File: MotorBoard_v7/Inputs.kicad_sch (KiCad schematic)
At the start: 5 parts, among them J13 Bump_Left, J14 Bump_Center, J15 Bump_Right, U5 ESP8266-1

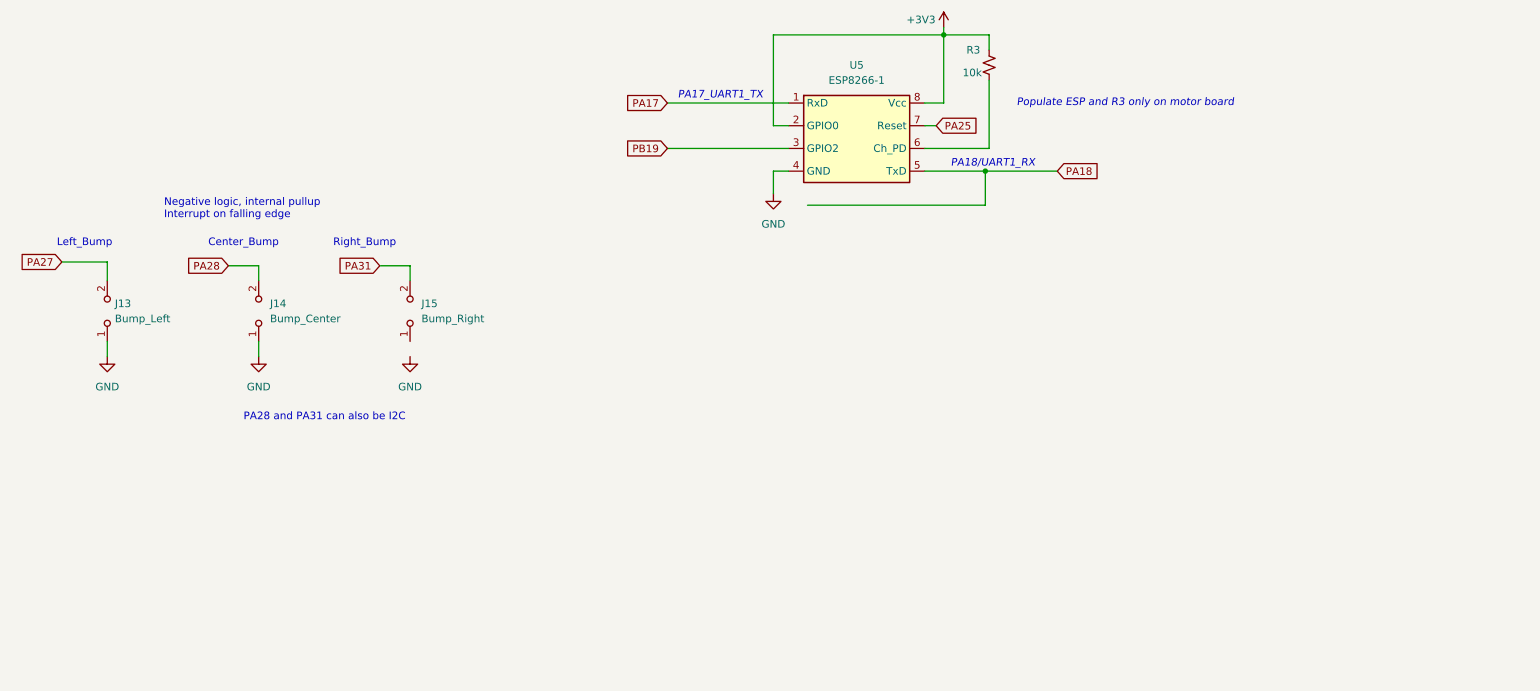
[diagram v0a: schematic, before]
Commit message: added lab 6 update starter files
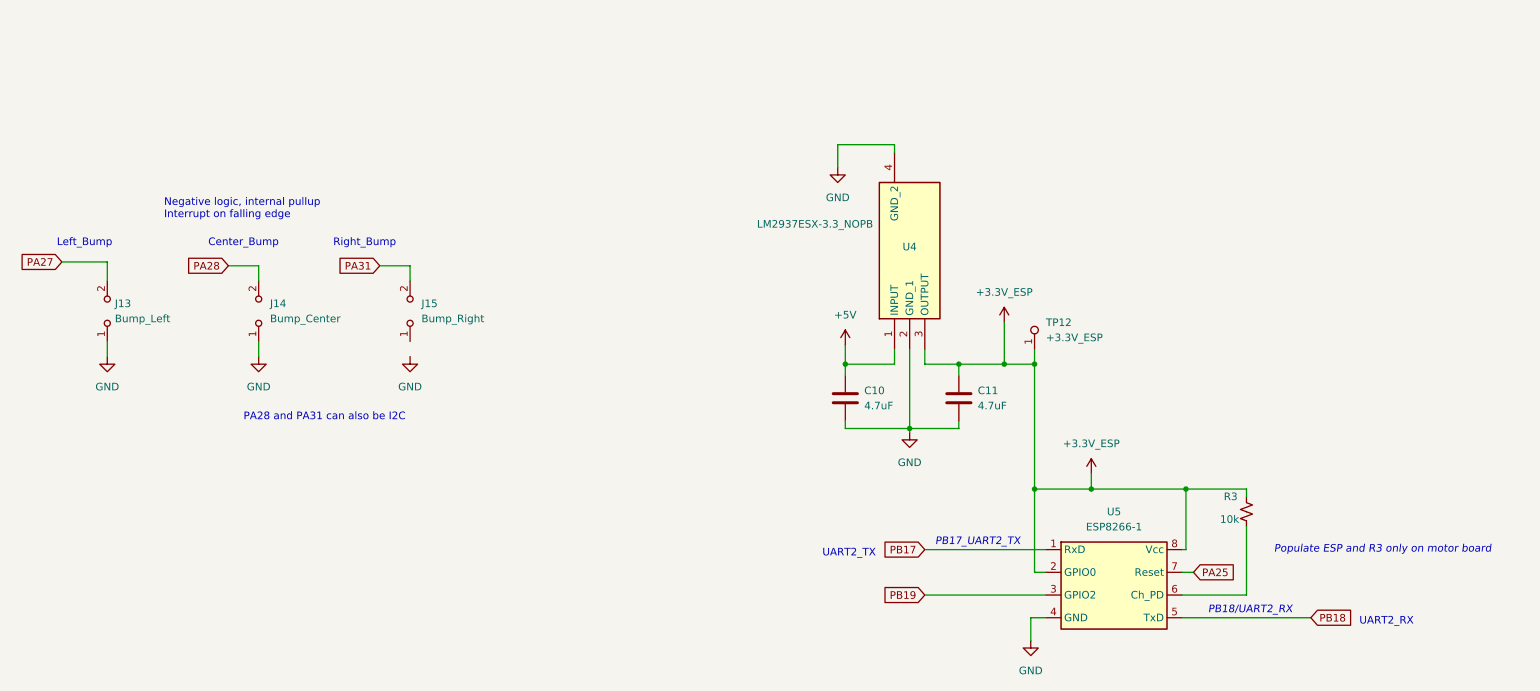
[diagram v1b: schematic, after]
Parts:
- added C10, C11: 4.7uF, ECE445L:C_0805_2012Metric, symbol ECE445L:C_0805
- added TP12: +3.3V_ESP, ECE445L:Testpoint_1x1, symbol ECE445L:Testpoint_1
- added U4: LM2937ESX-3.3_NOPB, ECE445L:SOT230P700X180-4N, symbol ECE445L:LM2937IMP-3.3_NOPB
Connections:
- net GND: now also C10.2, C11.2, U4.2 (GND_1), U4.4 (GND_2)
- net +3V3 renamed +3.3V_ESP
- net +3.3V_ESP: now also C11.1, TP12.1 (A), U4.3 (OUTPUT)
- net PA17 renamed PB17
- net PA18 renamed PB18
- new net +5V: C10.1, U4.1 (INPUT)
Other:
- note added: "PB17_UART2_TX"
- note added: "PB18/UART2_RX"
- note added: "UART2_RX"
- note added: "UART2_TX"
- note removed: "PA17_UART1_TX"
- note removed: "PA18/UART1_RX"
- moved on the sheet: R3, U5
